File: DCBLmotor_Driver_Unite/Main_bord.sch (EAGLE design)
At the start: 72 parts, among them CN1 DF11-16DP-2DSA, CN2 DF11-16DP-2DSA, CN3 DF11-4DP-2DSR, CN4 HIF3FC-10PA-2.54DSA(71), CN5 HIF3FC-10PA-2.54DSA(71), CN6 0430450612, CN7 0430450612, CN8 BM11B-SRSS-TB, IC1 TMPM370FYFG, IC2 MCP2561FD-E/MF, IC3 AM26C32CD, IC4 AM26C32CD, IC5 LTC2862A, SW1 CVS-02TB, SW2 EVQ-PE104K

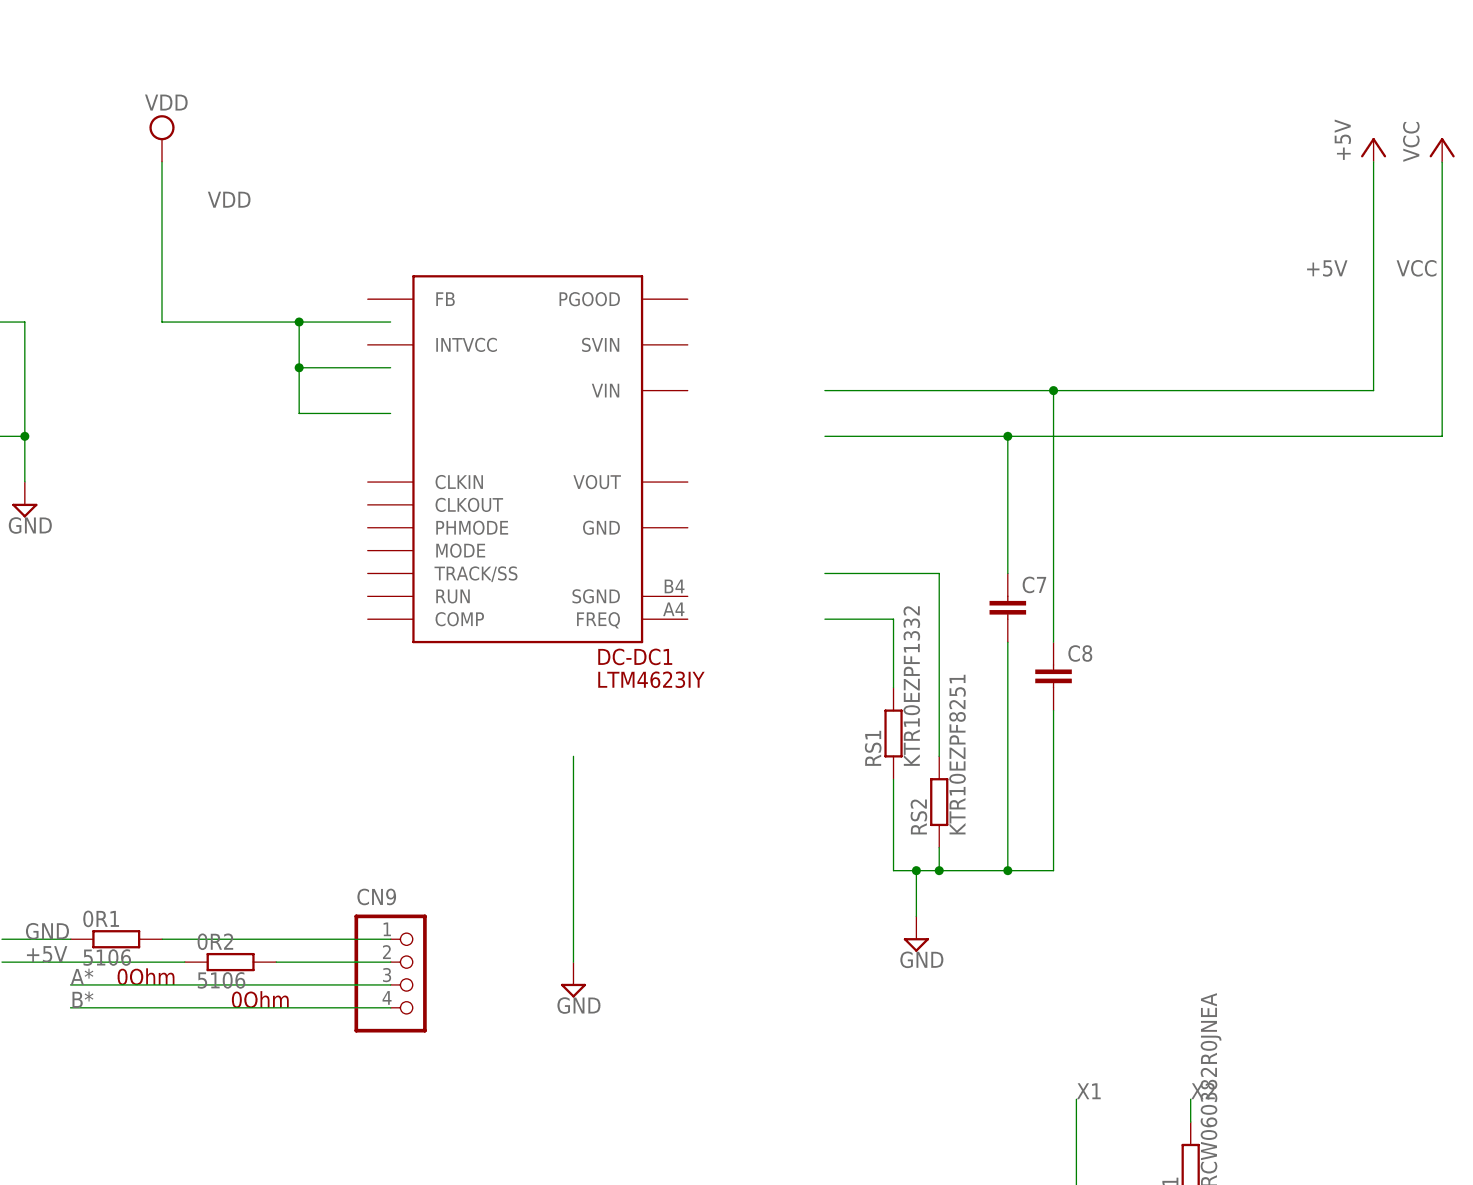
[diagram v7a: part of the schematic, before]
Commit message: Add LTM4623
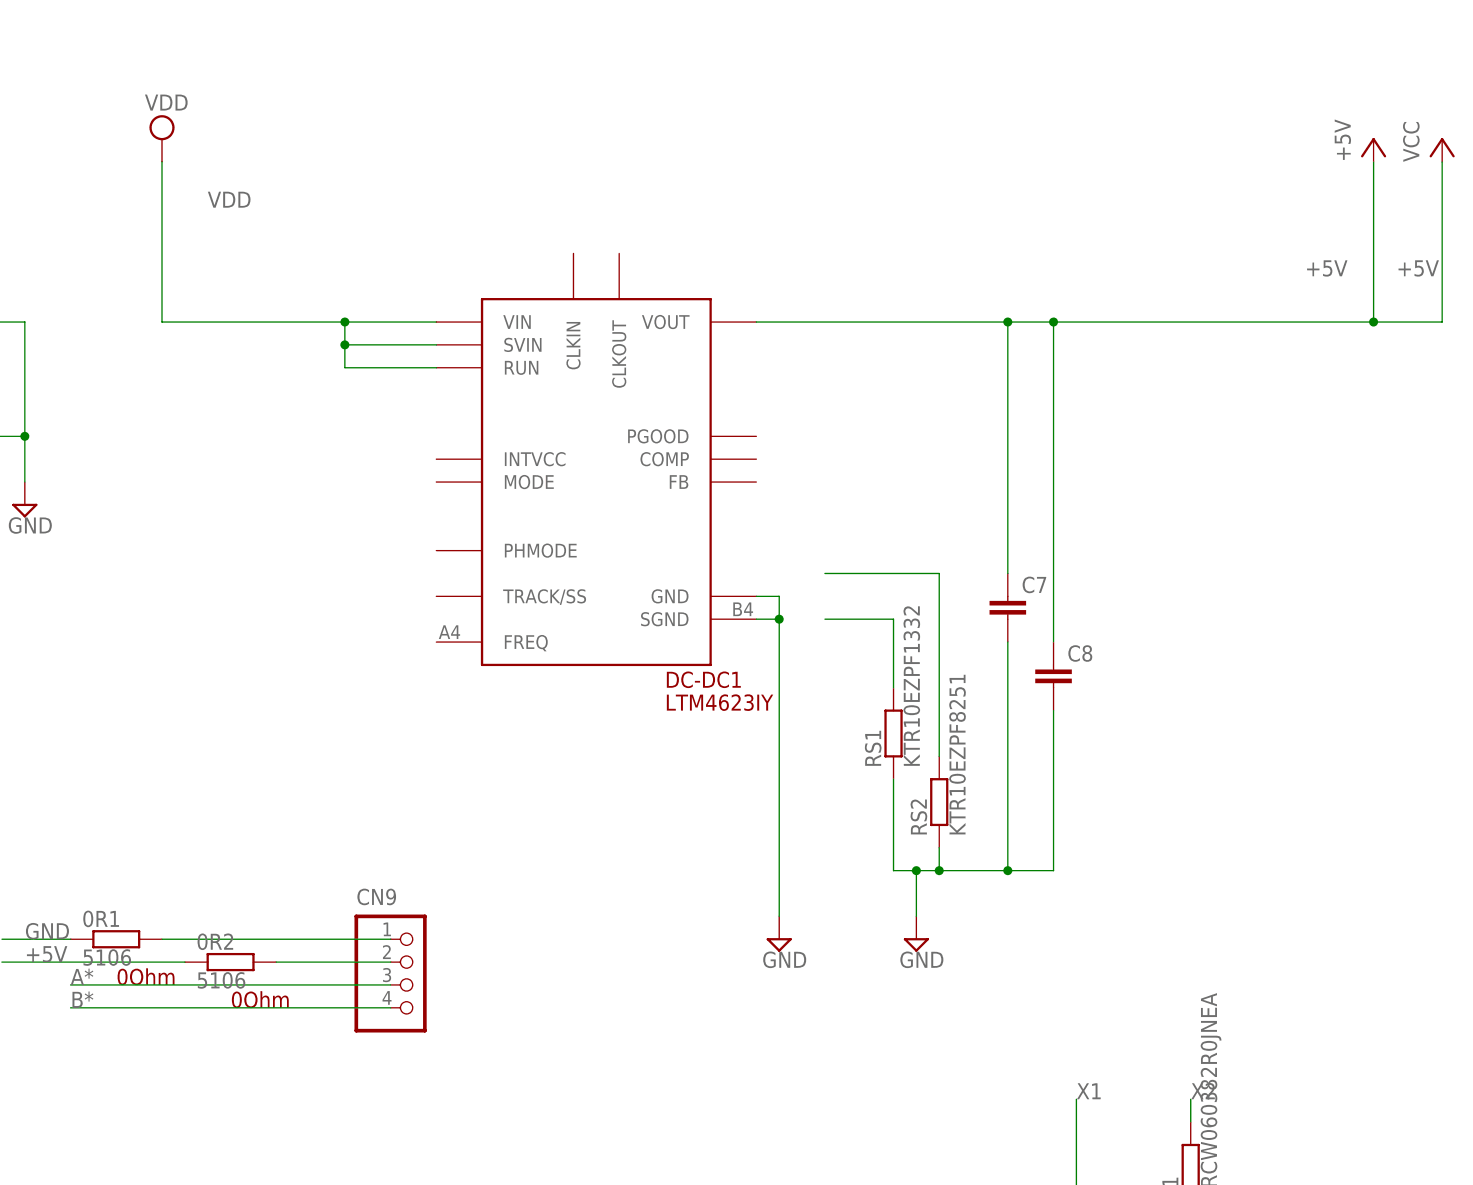
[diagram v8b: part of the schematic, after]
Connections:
- net +5V: now also C7.1, DC-DC1.VOUT
- net GND: now also DC-DC1.GND, DC-DC1.SGND
- net VCC: no longer C7.1
- net VDD: now also DC-DC1.RUN, DC-DC1.SVIN, DC-DC1.VIN
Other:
- moved on the sheet: DC-DC1
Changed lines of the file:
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@@
 <instance part="SUPPLY1" gate="GND" x="40.64" y="142.24"/>
 <instance part="SUPPLY2" gate="GND" x="231.14" y="20.32"/>
-<instance part="SUPPLY3" gate="GND" x="393.7" y="-22.86"/>
+<instance part="SUPPLY3" gate="GND" x="416.56" y="-17.78"/>
 <instance part="SUPPLY5" gate="GND" x="78.74" y="-127"/>
 <instance part="RS1" gate="G$1" x="429.26" y="5.08" rot="R90"/>
@@
 <instance part="CN10" gate="G$1" x="467.36" y="220.98"/>
 <instance part="C5" gate="G$1" x="439.42" y="220.98"/>
-<instance part="DC-DC1" gate="G$1" x="388.62" y="35.56"/>
+<instance part="DC-DC1" gate="G$1" x="396.24" y="33.02"/>
 </instances>
 <busses>
@@
 </net>
 <net name="GND" class="0">
-<segment>
-<pinref part="SUPPLY3" gate="GND" pin="GND"/>
-<wire x1="393.7" y1="2.54" x2="393.7" y2="-20.32" width="0.1524" layer="91"/>
-</segment>
 <segment>
 <pinref part="RS1" gate="G$1" pin="2"/>
@@
 <junction x="454.66" y="213.36"/>
 </segment>
+<segment>
+<pinref part="DC-DC1" gate="G$1" pin="GND"/>
+<wire x1="414.02" y1="20.32" x2="416.56" y2="20.32" width="0.1524" layer="91"/>
+<wire x1="416.56" y1="20.32" x2="416.56" y2="17.78" width="0.1524" layer="91"/>
+<pinref part="DC-DC1" gate="G$1" pin="SGND"/>
+<wire x1="414.02" y1="17.78" x2="416.56" y2="17.78" width="0.1524" layer="91"/>
+<junction x="416.56" y="17.78"/>
+<pinref part="SUPPLY3" gate="GND" pin="GND"/>
+<wire x1="416.56" y1="-15.24" x2="416.56" y2="17.78" width="0.1524" layer="91"/>
+</segment>
 </net>
 <net name="N$7" class="0">
@@
 <net name="VCC" class="0">
 <segment>
-<pinref part="P+6" gate="VCC" pin="VCC"/>
-<wire x1="490.22" y1="68.58" x2="490.22" y2="38.1" width="0.1524" layer="91"/>
-<label x="485.14" y="55.88" size="1.778" layer="95"/>
-<wire x1="441.96" y1="38.1" x2="490.22" y2="38.1" width="0.1524" layer="91"/>
-<pinref part="C7" gate="G$1" pin="1"/>
-<wire x1="441.96" y1="22.86" x2="441.96" y2="38.1" width="0.1524" layer="91"/>
-<wire x1="441.96" y1="38.1" x2="421.64" y2="38.1" width="0.1524" layer="91"/>
-<junction x="441.96" y="38.1"/>
-</segment>
-<segment>
 <pinref part="R2" gate="G$1" pin="1"/>
 <pinref part="P+9" gate="VCC" pin="VCC"/>
@@
 <segment>
 <pinref part="P+7" gate="VCC" pin="VCC"/>
-<wire x1="482.6" y1="68.58" x2="482.6" y2="43.18" width="0.1524" layer="91"/>
+<wire x1="482.6" y1="68.58" x2="482.6" y2="50.8" width="0.1524" layer="91"/>
 <label x="474.98" y="55.88" size="1.778" layer="95"/>
 <pinref part="C8" gate="G$1" pin="1"/>
-<wire x1="421.64" y1="43.18" x2="447.04" y2="43.18" width="0.1524" layer="91"/>
-<wire x1="447.04" y1="43.18" x2="447.04" y2="15.24" width="0.1524" layer="91"/>
-<junction x="447.04" y="43.18"/>
-<wire x1="447.04" y1="43.18" x2="482.6" y2="43.18" width="0.1524" layer="91"/>
+<wire x1="447.04" y1="50.8" x2="447.04" y2="15.24" width="0.1524" layer="91"/>
+<pinref part="DC-DC1" gate="G$1" pin="VOUT"/>
+<wire x1="414.02" y1="50.8" x2="441.96" y2="50.8" width="0.1524" layer="91"/>
+<wire x1="441.96" y1="50.8" x2="447.04" y2="50.8" width="0.1524" layer="91"/>
+<wire x1="447.04" y1="50.8" x2="482.6" y2="50.8" width="0.1524" layer="91"/>
+<junction x="447.04" y="50.8"/>
+<pinref part="P+6" gate="VCC" pin="VCC"/>
+<wire x1="490.22" y1="68.58" x2="490.22" y2="50.8" width="0.1524" layer="91"/>
+<label x="485.14" y="55.88" size="1.778" layer="95"/>
+<wire x1="482.6" y1="50.8" x2="490.22" y2="50.8" width="0.1524" layer="91"/>
+<junction x="482.6" y="50.8"/>
+<pinref part="C7" gate="G$1" pin="1"/>
+<wire x1="441.96" y1="22.86" x2="441.96" y2="50.8" width="0.1524" layer="91"/>
+<junction x="441.96" y="50.8"/>
 </segment>
 <segment>
@@
 <wire x1="347.98" y1="68.58" x2="347.98" y2="50.8" width="0.1524" layer="91"/>
 <label x="353.06" y="63.5" size="1.778" layer="95"/>
-<wire x1="373.38" y1="50.8" x2="363.22" y2="50.8" width="0.1524" layer="91"/>
-<wire x1="363.22" y1="50.8" x2="347.98" y2="50.8" width="0.1524" layer="91"/>
-<wire x1="373.38" y1="40.64" x2="363.22" y2="40.64" width="0.1524" layer="91"/>
-<wire x1="363.22" y1="40.64" x2="363.22" y2="45.72" width="0.1524" layer="91"/>
-<junction x="363.22" y="50.8"/>
-<wire x1="363.22" y1="45.72" x2="363.22" y2="50.8" width="0.1524" layer="91"/>
-<wire x1="373.38" y1="45.72" x2="363.22" y2="45.72" width="0.1524" layer="91"/>
-<junction x="363.22" y="45.72"/>
-</segment>
-<segment>
+<wire x1="378.46" y1="50.8" x2="368.3" y2="50.8" width="0.1524" layer="91"/>
+<pinref part="DC-DC1" gate="G$1" pin="VIN"/>
+<pinref part="DC-DC1" gate="G$1" pin="SVIN"/>
+<wire x1="368.3" y1="50.8" x2="347.98" y2="50.8" width="0.1524" layer="91"/>
+<wire x1="378.46" y1="48.26" x2="368.3" y2="48.26" width="0.1524" layer="91"/>
+<wire x1="368.3" y1="48.26" x2="368.3" y2="50.8" width="0.1524" layer="91"/>
+<junction x="368.3" y="50.8"/>
+<pinref part="DC-DC1" gate="G$1" pin="RUN"/>
+<wire x1="378.46" y1="45.72" x2="368.3" y2="45.72" width="0.1524" layer="91"/>
+<wire x1="368.3" y1="45.72" x2="368.3" y2="48.26" width="0.1524" layer="91"/>
+<junction x="368.3" y="48.26"/>
+</segment>
+<segment>
